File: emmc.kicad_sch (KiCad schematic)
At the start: 30 parts, among them U901 MX52LM04A11XSI

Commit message: minor formatting updates
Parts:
- renumbered C905 to C901, C906 to C902, C901 to C905, C902 to C906, R920 to R904, R904 to R905, R905 to R906, R906 to R907, R907 to R908, R908 to R909, R918 to R910, R921 to R911, R909 to R912, R910 to R913, R911 to R914, R912 to R915, R913 to R916, R914 to R917, R915 to R918, R916 to R919, R917 to R920, R919 to R921

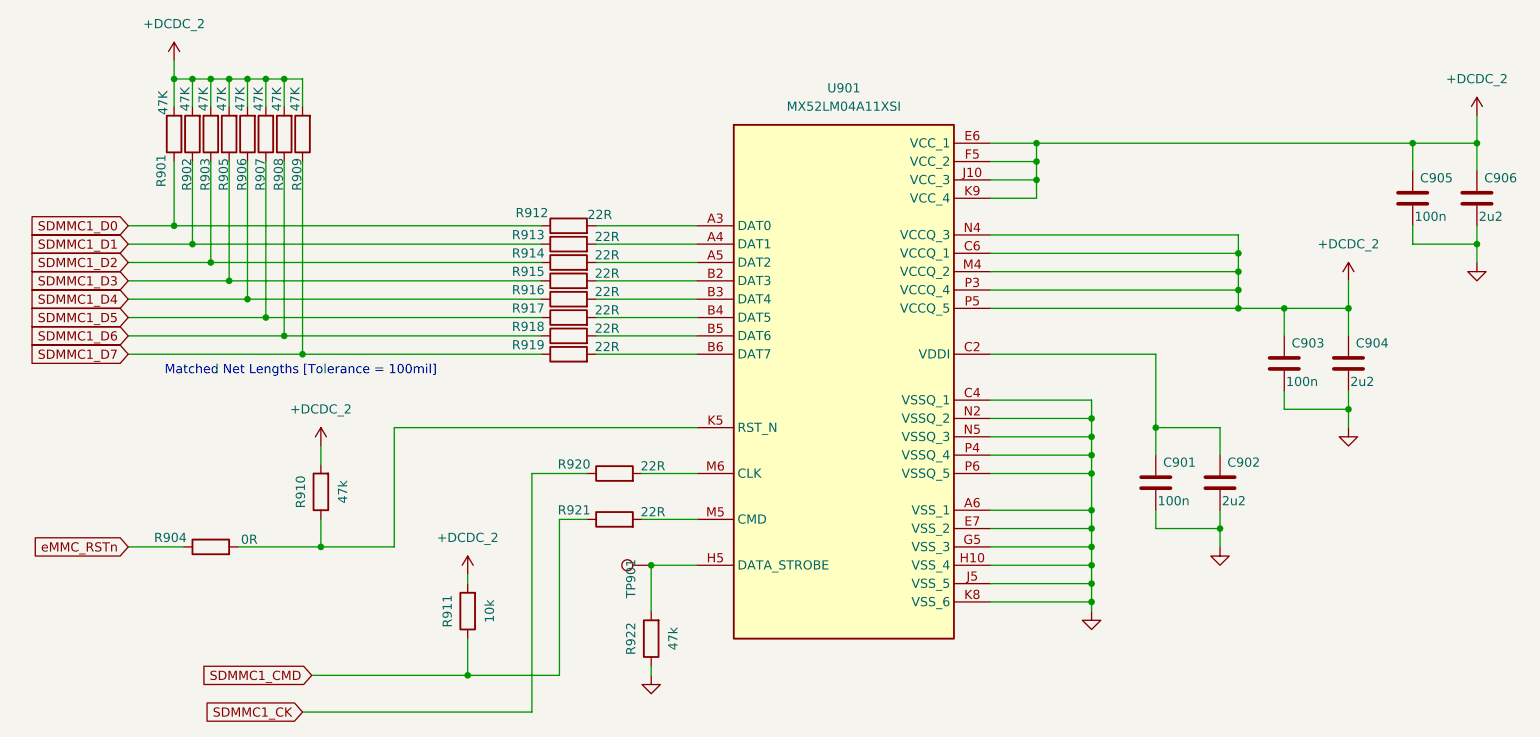
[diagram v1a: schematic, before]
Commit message: schematics errors fixed and ready for PCB
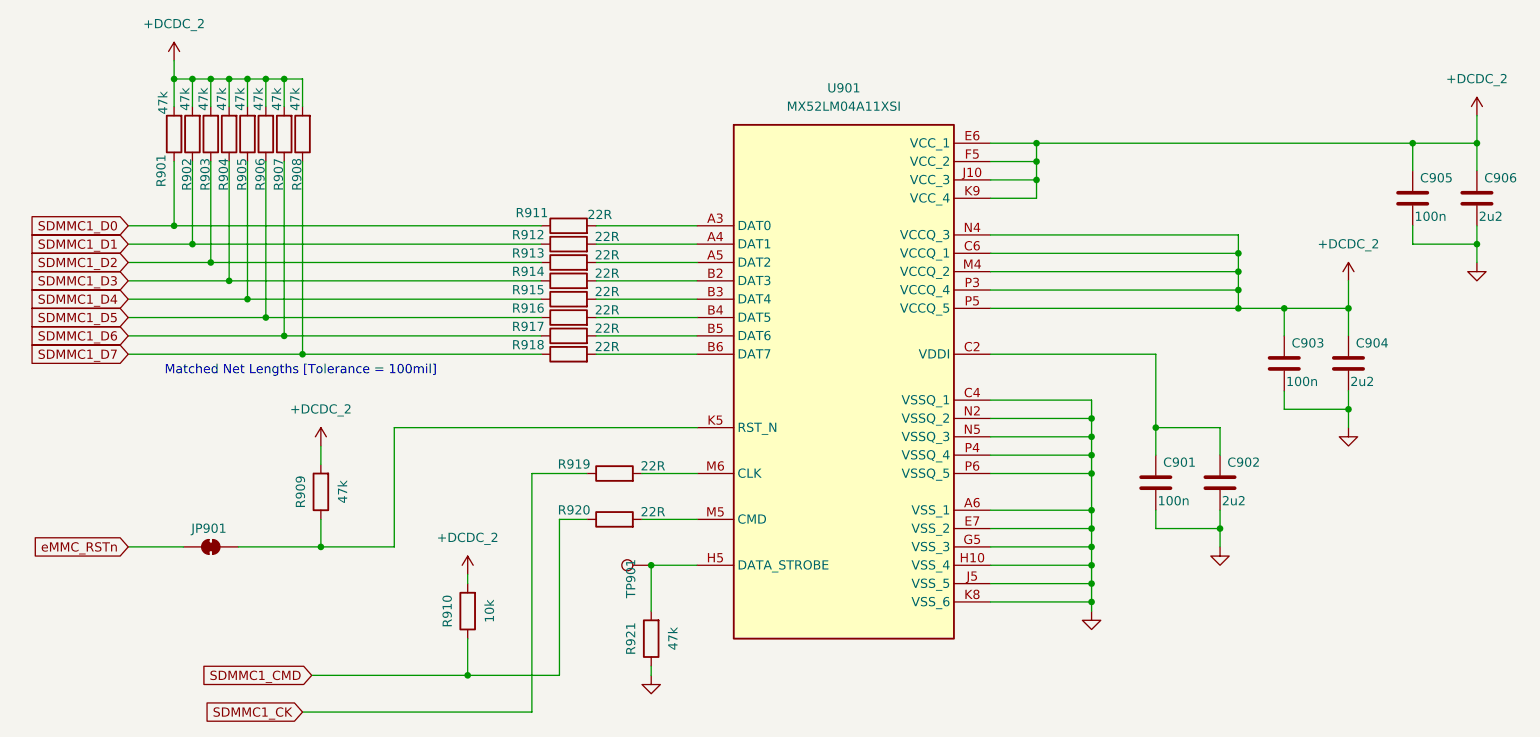
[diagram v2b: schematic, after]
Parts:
- removed R904: 0R, symbol Device:R
- added JP901: SolderJumper_2_Bridged, Jumper:SolderJumper-2_P1.3mm_Bridged_RoundedPad1.0x1.5mm, symbol Jumper:SolderJumper_2_Bridged
- C901, C903, C905: footprint (none) -> Capacitor_SMD:C_0402_1005Metric; Distributor_Link (none) -> https://www.mouser.com/ProductDetail/KYOCERA-AVX/04023C104K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; Manufacturer_Name (none) -> KYOCERA AVX; Manufacturer_Part_Number (none) -> 04023C104KAT2A
- C902, C904, C906: footprint (none) -> Capacitor_SMD:C_0402_1005Metric; Distributor_Link (none) -> https://www.mouser.com/ProductDetail/KYOCERA-AVX/KGM05AR51A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; Manufacturer_Name (none) -> KYOCERA AVX; Manufacturer_Part_Number (none) -> 04023C104KAT2A
- R901, R902, R903: value 47K -> 47k; footprint (none) -> Resistor_SMD:R_0603_1608Metric; Distributor_Link (none) -> https://www.mouser.com/ProductDetail/Vishay-Dale/CRCW060347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; Manufacturer_Name (none) -> Vishay/Dale; Manufacturer_Part_Number (none) -> CRCW060347K0FKEAHP
- R904: renamed from R905; value 47K -> 47k; footprint (none) -> Resistor_SMD:R_0603_1608Metric; Distributor_Link (none) -> https://www.mouser.com/ProductDetail/Vishay-Dale/CRCW060347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; Manufacturer_Name (none) -> Vishay/Dale; Manufacturer_Part_Number (none) -> CRCW060347K0FKEAHP
- R905: renamed from R906; value 47K -> 47k; footprint (none) -> Resistor_SMD:R_0603_1608Metric; Distributor_Link (none) -> https://www.mouser.com/ProductDetail/Vishay-Dale/CRCW060347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; Manufacturer_Name (none) -> Vishay/Dale; Manufacturer_Part_Number (none) -> CRCW060347K0FKEAHP
- R906: renamed from R907; value 47K -> 47k; footprint (none) -> Resistor_SMD:R_0603_1608Metric; Distributor_Link (none) -> https://www.mouser.com/ProductDetail/Vishay-Dale/CRCW060347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; Manufacturer_Name (none) -> Vishay/Dale; Manufacturer_Part_Number (none) -> CRCW060347K0FKEAHP
- R907: renamed from R908; value 47K -> 47k; footprint (none) -> Resistor_SMD:R_0603_1608Metric; Distributor_Link (none) -> https://www.mouser.com/ProductDetail/Vishay-Dale/CRCW060347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; Manufacturer_Name (none) -> Vishay/Dale; Manufacturer_Part_Number (none) -> CRCW060347K0FKEAHP
- R908: renamed from R909; value 47K -> 47k; footprint (none) -> Resistor_SMD:R_0603_1608Metric; Distributor_Link (none) -> https://www.mouser.com/ProductDetail/Vishay-Dale/CRCW060347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; Manufacturer_Name (none) -> Vishay/Dale; Manufacturer_Part_Number (none) -> CRCW060347K0FKEAHP
- R909: renamed from R910; footprint (none) -> Resistor_SMD:R_0603_1608Metric; Distributor_Link (none) -> https://www.mouser.com/ProductDetail/Vishay-Dale/CRCW060347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; Manufacturer_Name (none) -> Vishay/Dale; Manufacturer_Part_Number (none) -> CRCW060347K0FKEAHP
- R910: renamed from R911; footprint (none) -> Resistor_SMD:R_0603_1608Metric; Distributor_Link (none) -> https://www.mouser.com/ProductDetail/Vishay-Dale/CRCW060310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; Manufacturer_Name (none) -> Vishay/Dale; Manufacturer_Part_Number (none) -> CRCW060310K0FKEI
- R911: renamed from R912; footprint (none) -> Resistor_SMD:R_0603_1608Metric; Distributor_Link (none) -> https://www.mouser.com/ProductDetail/Panasonic/ERJ-S03F22R0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; Manufacturer_Name (none) -> Panasonic; Manufacturer_Part_Number (none) -> ERJ-S03F22R0V
- R912: renamed from R913; footprint (none) -> Resistor_SMD:R_0603_1608Metric; Distributor_Link (none) -> https://www.mouser.com/ProductDetail/Panasonic/ERJ-S03F22R0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; Manufacturer_Name (none) -> Panasonic; Manufacturer_Part_Number (none) -> ERJ-S03F22R0V
- R913: renamed from R914; footprint (none) -> Resistor_SMD:R_0603_1608Metric; Distributor_Link (none) -> https://www.mouser.com/ProductDetail/Panasonic/ERJ-S03F22R0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; Manufacturer_Name (none) -> Panasonic; Manufacturer_Part_Number (none) -> ERJ-S03F22R0V
- R914: renamed from R915; footprint (none) -> Resistor_SMD:R_0603_1608Metric; Distributor_Link (none) -> https://www.mouser.com/ProductDetail/Panasonic/ERJ-S03F22R0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; Manufacturer_Name (none) -> Panasonic; Manufacturer_Part_Number (none) -> ERJ-S03F22R0V
- R915: renamed from R916; footprint (none) -> Resistor_SMD:R_0603_1608Metric; Distributor_Link (none) -> https://www.mouser.com/ProductDetail/Panasonic/ERJ-S03F22R0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; Manufacturer_Name (none) -> Panasonic; Manufacturer_Part_Number (none) -> ERJ-S03F22R0V
- R916: renamed from R917; footprint (none) -> Resistor_SMD:R_0603_1608Metric; Distributor_Link (none) -> https://www.mouser.com/ProductDetail/Panasonic/ERJ-S03F22R0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; Manufacturer_Name (none) -> Panasonic; Manufacturer_Part_Number (none) -> ERJ-S03F22R0V
- R917: renamed from R918; footprint (none) -> Resistor_SMD:R_0603_1608Metric; Distributor_Link (none) -> https://www.mouser.com/ProductDetail/Panasonic/ERJ-S03F22R0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; Manufacturer_Name (none) -> Panasonic; Manufacturer_Part_Number (none) -> ERJ-S03F22R0V
- R918: renamed from R919; footprint (none) -> Resistor_SMD:R_0603_1608Metric; Distributor_Link (none) -> https://www.mouser.com/ProductDetail/Panasonic/ERJ-S03F22R0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; Manufacturer_Name (none) -> Panasonic; Manufacturer_Part_Number (none) -> ERJ-S03F22R0V
- R919: renamed from R920; footprint (none) -> Resistor_SMD:R_0603_1608Metric; Distributor_Link (none) -> https://www.mouser.com/ProductDetail/Panasonic/ERJ-S03F22R0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; Manufacturer_Name (none) -> Panasonic; Manufacturer_Part_Number (none) -> ERJ-S03F22R0V
- R920: renamed from R921; footprint (none) -> Resistor_SMD:R_0603_1608Metric; Distributor_Link (none) -> https://www.mouser.com/ProductDetail/Panasonic/ERJ-S03F22R0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; Manufacturer_Name (none) -> Panasonic; Manufacturer_Part_Number (none) -> ERJ-S03F22R0V
- R921: renamed from R922; footprint (none) -> Resistor_SMD:R_0603_1608Metric; Distributor_Link (none) -> https://www.mouser.com/ProductDetail/Vishay-Dale/CRCW060347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; Manufacturer_Name (none) -> Vishay/Dale; Manufacturer_Part_Number (none) -> CRCW060347K0FKEAHP
- TP901: footprint (none) -> TestPoint:TestPoint_Pad_D3.0mm
- U901: Distributor_Link (none) -> https://www.mouser.com/ProductDetail/Macronix/MX52LM04A11XS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
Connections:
- net eMMC_RSTn: now also JP901.1 (A)
- net at R909.1, U901.K5 (RST_N): now also JP901.2 (B)

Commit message: new version created. Now at v2.0.0
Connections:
- net VDDI: now reaches C901.1, C902.1, U901.C2 (VDDI)
- net SDMMC1_D5_R: now reaches R916.2, U901.B4 (DAT5)
- net SDMMC1_eMMC_RSTn_JP: now reaches JP901.2 (B), R909.1, U901.K5 (RST_N)
- net SDMMC1_D1_R: now reaches R912.2, U901.A4 (DAT1)
- net SDMMC1_D3_R: now reaches R914.2, U901.B2 (DAT3)
- net SDMMC1_D2_R: now reaches R913.2, U901.A5 (DAT2)
- net SDMMC1_D7_R: now reaches R918.2, U901.B6 (DAT7)
- net SDMMC1_D0_R: now reaches R911.2, U901.A3 (DAT0)
- net SDMMC1_CMD_R: now reaches R919.2, U901.M6 (CLK)
- net SDMMC1_D4_R: now reaches R915.2, U901.B3 (DAT4)
- net SDMMC1_D6_R: now reaches R917.2, U901.B5 (DAT6)
- net SDMMC1_CK_R: now reaches R920.2, U901.M5 (CMD)
- net +DCDC_2 renamed +DCDC_1
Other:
- moved on the sheet: R911, R912, R913, R914, R915, R916, R917, R918, R919, R920

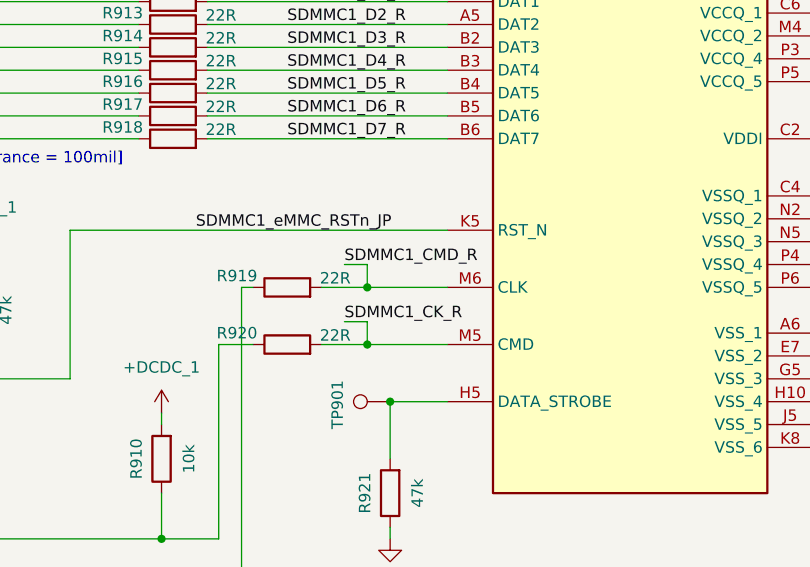
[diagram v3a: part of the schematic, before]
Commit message: optimized the eMMC routing
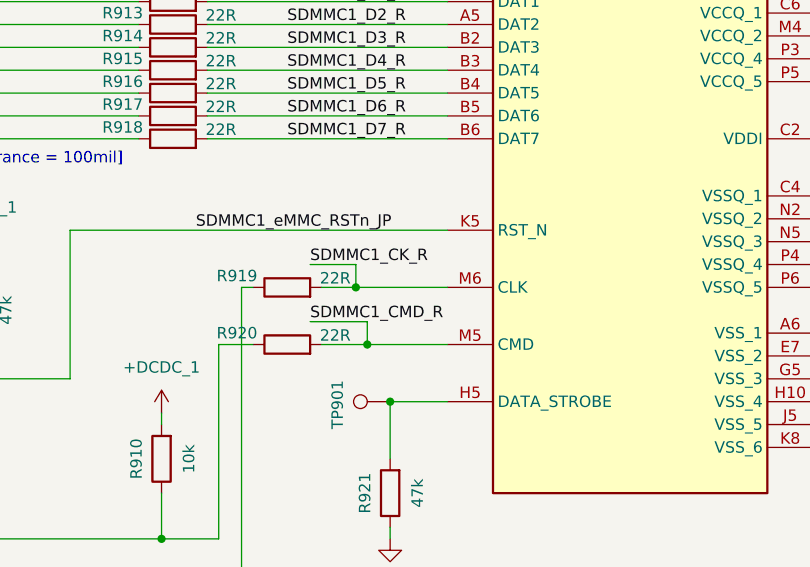
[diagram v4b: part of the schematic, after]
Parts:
- R901, R902, R903, R904, R905, R906, R907, R908, R909, R921: footprint Resistor_SMD:R_0603_1608Metric -> Resistor_SMD:R_0402_1005Metric; Distributor_Link https://www.mouser.com/ProductDetail/Vishay-Dale/CRCW060347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 -> https://www.mouser.com/ProductDetail/YAGEO/RC0402FR-7D47KL?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; Manufacturer_Name Vishay/Dale -> YAGEO; Manufacturer_Part_Number CRCW060347K0FKEAHP -> RC0402FR-7D47KL
- R910: footprint Resistor_SMD:R_0603_1608Metric -> Resistor_SMD:R_0402_1005Metric; Distributor_Link https://www.mouser.com/ProductDetail/Vishay-Dale/CRCW060310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 -> https://www.mouser.com/ProductDetail/Panasonic/ERJ-PA2F1002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; Manufacturer_Name Vishay/Dale -> Panasonic; Manufacturer_Part_Number CRCW060310K0FKEI -> ERJ-PA2F1002X
- R911, R912, R913, R914, R915, R916, R917, R918, R919, R920: footprint Resistor_SMD:R_0603_1608Metric -> Resistor_SMD:R_0402_1005Metric; Distributor_Link https://www.mouser.com/ProductDetail/Panasonic/ERJ-S03F22R0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 -> https://www.mouser.com/ProductDetail/YAGEO/RC0402FR-7D22RL?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; Manufacturer_Name Panasonic -> YAGEO; Manufacturer_Part_Number ERJ-S03F22R0V -> RC0402FR-7D22RL
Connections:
- net SDMMC1_CK_R: now also R919.2, U901.M6 (CLK); no longer R920.2, U901.M5 (CMD)
- net SDMMC1_CMD_R: now also R920.2, U901.M5 (CMD); no longer R919.2, U901.M6 (CLK)

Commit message: minor design improvements
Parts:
- removed JP901: SolderJumper_2_Bridged, Jumper:SolderJumper-2_P1.3mm_Bridged_RoundedPad1.0x1.5mm, symbol Jumper:SolderJumper_2_Bridged
- added R922: 0R, Resistor_SMD:R_0603_1608Metric, symbol Device:R
- C902, C904, C906: Manufacturer_Part_Number 04023C104KAT2A -> KGM05AR51A225KH
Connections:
- net SDMMC1_eMMC_RSTn_JP: now also R922.2
- net eMMC_RSTn: now also R922.1
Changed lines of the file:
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@@
 	(wire
 		(pts
+			(xy 67.31 116.84) (xy 77.47 116.84)
+		)
+		(stroke
+			(width 0)
+			(type default)
+		)
+	)
+	(wire
+		(pts
 			(xy 210.82 83.82) (xy 210.82 87.63)
 		)
@@
 	(wire
 		(pts
-			(xy 50.8 116.84) (xy 58.42 116.84)
+			(xy 50.8 116.84) (xy 59.69 116.84)
 		)
 		(stroke
@@
 	(wire
 		(pts
-			(xy 66.04 116.84) (xy 77.47 116.84)
-		)
-		(stroke
-			(width 0)
-			(type default)
-		)
-	)
-	(wire
-		(pts
 			(xy 114.3 110.49) (xy 120.65 110.49)
 		)
@@
 			)
 		)
-		(property "Manufacturer_Part_Number" "04023C104KAT2A"
+		(property "Manufacturer_Part_Number" "KGM05AR51A225KH"
 			(at 201.93 107.95 0)
 			(effects
@@
 			)
 		)
-		(property "Manufacturer_Part_Number" "04023C104KAT2A"
+		(property "Manufacturer_Part_Number" "KGM05AR51A225KH"
 			(at 219.71 91.44 0)
 			(effects
@@
 	(symbol
 		(lib_id "Device:R")
+		(at 63.5 116.84 90)
+		(unit 1)
+		(exclude_from_sim no)
+		(in_bom yes)
+		(on_board yes)
+		(dnp no)
+		(property "Reference" "R922"
+			(at 56.896 114.046 90)
+			(effects
+				(font
+					(size 1.27 1.27)
+				)
+			)
+		)
+		(property "Value" "0R"
+			(at 63.754 114.046 90)
+			(effects
+				(font
+					(size 1.27 1.27)
+				)
+			)
+		)
+		(property "Footprint" "Resistor_SMD:R_0603_1608Metric"
+			(at 63.5 118.618 90)
+			(effects
+				(font
+					(size 1.27 1.27)
+				)
+				(hide yes)
+			)
+		)
+		(property "Datasheet" "https://www.vishay.com/doc?20035https://www.vishay.com/doc?20035"
+			(at 63.5 116.84 0)
+			(effects
+				(font
+					(size 1.27 1.27)
+				)
+				(hide yes)
+			)
+		)
+		(property "Description" "Resistor"
+			(at 63.5 116.84 0)
+			(effects
+				(font
+					(size 1.27 1.27)
+				)
+				(hide yes)
+			)
+		)
+		(property "Distributor_Link" "https://www.mouser.com/ProductDetail/Vishay/CRCW06030000Z0EI?qs=%252B6g0mu59x7L7KQG%252Bwwt0jQ%3D%3D"
+			(at 63.5 116.84 0)
+			(effects
+				(font
+					(size 1.27 1.27)
+				)
+				(hide yes)
+			)
+		)
+		(property "Manufacturer_Name" "Vishay"
+			(at 63.5 116.84 0)
+			(effects
+				(font
+					(size 1.27 1.27)
+				)
+				(hide yes)
+			)
+		)
+		(property "Manufacturer_Part_Number" "CRCW06030000Z0EI"
+			(at 63.5 116.84 0)
+			(effects
+				(font
+					(size 1.27 1.27)
+				)
+				(hide yes)
+			)
+		)
+		(pin "2"
+		)
+		(pin "1"
+		)
+		(instances
+			(project "EnergyMonitoringSystem"
+				(path "/e660428c-c9b7-476c-8ac8-2d419f233469/abbcaca0-0b45-4de8-86ef-a8249be36b44"
+					(reference "R922")
+					(unit 1)
+				)
+			)
+		)
+	)
+	(symbol
+		(lib_id "Device:R")
 		(at 99.06 85.09 90)
 		(unit 1)
@@
 			)
 		)
-		(property "Manufacturer_Part_Number" "04023C104KAT2A"
+		(property "Manufacturer_Part_Number" "KGM05AR51A225KH"
 			(at 237.49 68.58 0)
 			(effects
@@
 					(unit 1)
 				)
-			)
-		)
-	)
-	(symbol
-		(lib_id "Jumper:SolderJumper_2_Bridged")
-		(at 62.23 116.84 0)
-		(unit 1)
-		(exclude_from_sim yes)
-		(in_bom no)
-		(on_board yes)
-		(dnp no)
-		(property "Reference" "JP901"
-			(at 61.976 114.3 0)
-			(effects
-				(font
-					(size 1.27 1.27)
-				)
-			)
-		)
-		(property "Value" "SolderJumper_2_Bridged"
-			(at 62.23 113.03 0)
-			(effects
-				(font
-					(size 1.27 1.27)
-				)
-				(hide yes)
-			)
-		)
-		(property "Footprint" "Jumper:SolderJumper-2_P1.3mm_Bridged_RoundedPad1.0x1.5mm"
-			(at 62.23 116.84 0)
-			(effects
-				(font
-					(size 1.27 1.27)
-				)
-				(hide yes)
-			)
-		)
-		(property "Datasheet" "~"
-			(at 62.23 116.84 0)
-			(effects
-				(font
-					(size 1.27 1.27)
-				)
-				(hide yes)
-			)
-		)
-		(property "Description" "Solder Jumper, 2-pole, closed/bridged"
-			(at 62.23 116.84 0)
-			(effects
-				(font
-					(size 1.27 1.27)
-				)
-				(hide yes)
-			)
-		)
-		(pin "1"
-		)
-		(pin "2"
-		)
-		(instances
-			(project "EnergyMonitoringSystem"
-				(path "/e660428c-c9b7-476c-8ac8-2d419f233469/abbcaca0-0b45-4de8-86ef-a8249be36b44"
-					(reference "JP901")
-					(unit 1)
-				)
